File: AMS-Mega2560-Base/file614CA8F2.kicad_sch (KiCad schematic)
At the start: 22 parts, among them IC13 MAX764CPA+, IC14 LM2917N-8_NOPB, J23 Conn_01x02, J24 Conn_01x02, J31 Conn_01x02, K1 DIP05-1A72-12L, Q25 2N7000

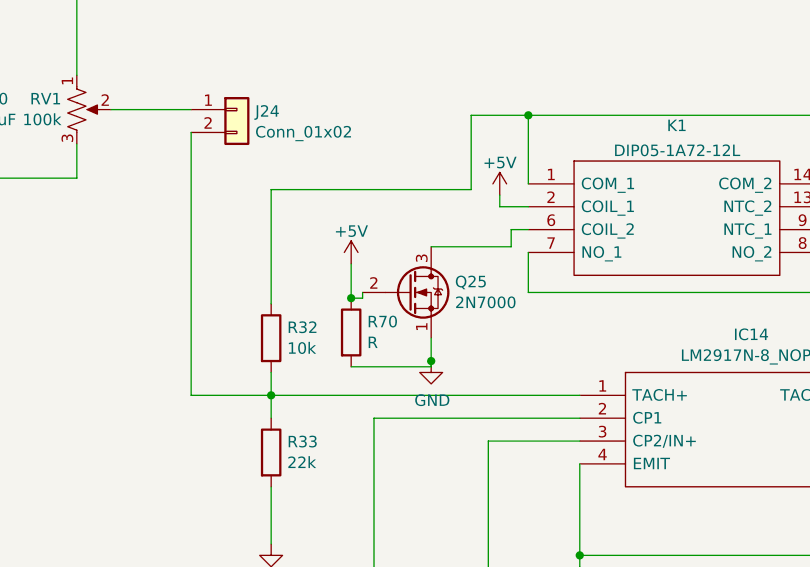
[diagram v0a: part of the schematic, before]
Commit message: applying some fixes for the RPM sensor and other parts of the schem
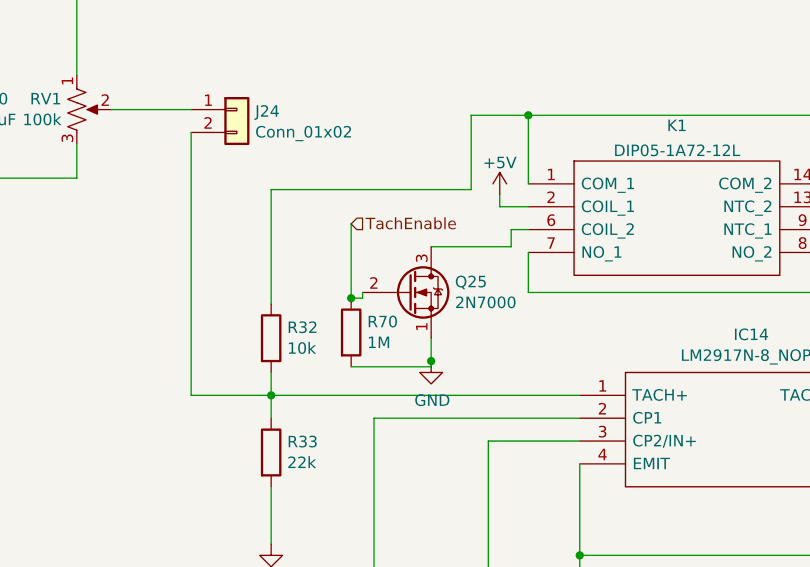
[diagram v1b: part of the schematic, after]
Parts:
- R70: value R -> 1M
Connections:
- net +5V: no longer Q25.2 (G), R70.1
- new net TachEnable: Q25.2 (G), R70.1
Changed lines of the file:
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@@
     (stroke (width 0) (type default) (color 0 0 0 0))
   )
-  (wire (pts (xy 161.29 79.375) (xy 161.29 83.185))
+  (wire (pts (xy 161.29 74.93) (xy 161.29 83.185))
     (stroke (width 0) (type default) (color 0 0 0 0))
   )
@@
   )
   (hierarchical_label "TachIn" (shape input) (at 219.075 78.105 0)
+    (effects (font (size 1.27 1.27)) (justify left))
+  )
+  (hierarchical_label "TachEnable" (shape input) (at 161.29 74.93 0)
     (effects (font (size 1.27 1.27)) (justify left))
   )
@@
       (effects (font (size 1.27 1.27)) (justify left))
     )
-    (property "Value" "R" (id 1) (at 163.068 88.138 0)
+    (property "Value" "1M" (id 1) (at 163.068 88.138 0)
       (effects (font (size 1.27 1.27)) (justify left))
     )
@@
     (pin "9")
   )
-  (symbol (lib_id "power:+5V") (at 161.29 79.375 0) (unit 1)
-    (in_bom yes) (on_board yes) (fields_autoplaced)
-    (property "Reference" "#PWR038" (id 0) (at 161.29 83.185 0)
-      (effects (font (size 1.27 1.27)) hide)
-    )
-    (property "Value" "+5V" (id 1) (at 161.29 75.7705 0))
-    (property "Footprint" "" (id 2) (at 161.29 79.375 0)
-      (effects (font (size 1.27 1.27)) hide)
-    )
-    (property "Datasheet" "" (id 3) (at 161.29 79.375 0)
-      (effects (font (size 1.27 1.27)) hide)
-    )
-    (pin "1")
-  )
 )

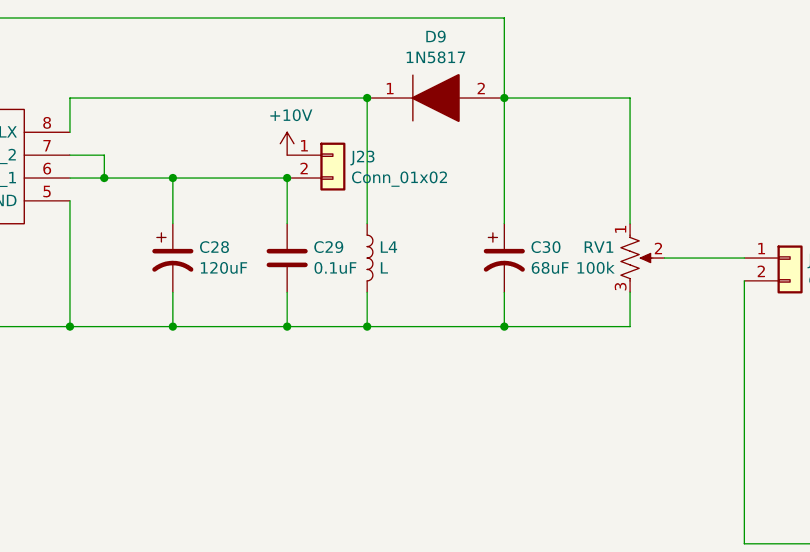
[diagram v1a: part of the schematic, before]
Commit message: updating some values and footprints. needs to have the routing tweaked
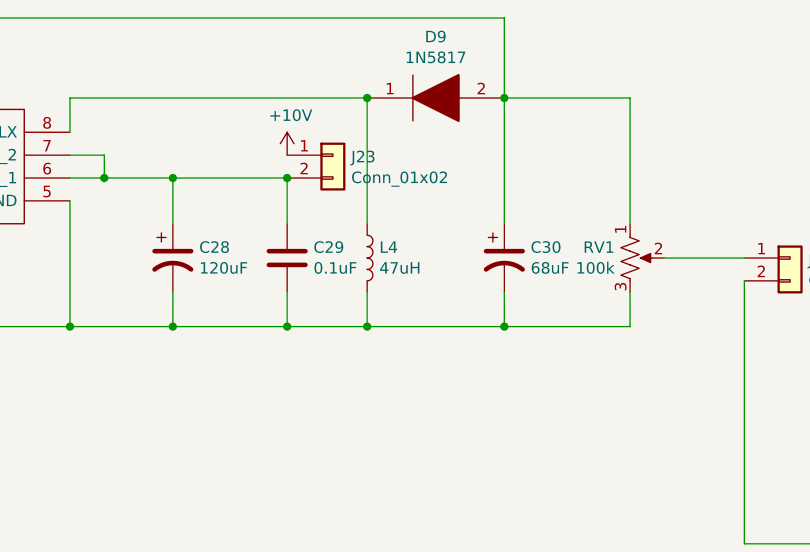
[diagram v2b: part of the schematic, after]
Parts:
- C28, C30: footprint Capacitor_THT:CP_Radial_D10.0mm_P5.00mm -> Capacitor_THT:CP_Radial_D8.0mm_P5.00mm
- C32: footprint Capacitor_THT:CP_Radial_D7.5mm_P2.50mm -> Capacitor_THT:C_Radial_D4.0mm_H5.0mm_P1.50mm
- L4: value L -> 47uH
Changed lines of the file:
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@@
       (effects (font (size 1.27 1.27)) (justify left))
     )
-    (property "Footprint" "Capacitor_THT:CP_Radial_D10.0mm_P5.00mm" (id 2) (at 116.84 62.23 0)
+    (property "Footprint" "Capacitor_THT:CP_Radial_D8.0mm_P5.00mm" (id 2) (at 116.84 62.23 0)
       (effects (font (size 1.27 1.27)) hide)
     )
@@
       (effects (font (size 1.27 1.27)) (justify left))
     )
-    (property "Footprint" "Capacitor_THT:CP_Radial_D10.0mm_P5.00mm" (id 2) (at 80.01 62.23 0)
+    (property "Footprint" "Capacitor_THT:CP_Radial_D8.0mm_P5.00mm" (id 2) (at 80.01 62.23 0)
       (effects (font (size 1.27 1.27)) hide)
     )
@@
       (effects (font (size 1.27 1.27)) (justify left))
     )
-    (property "Value" "L" (id 1) (at 102.9462 63.373 0)
+    (property "Value" "47uH" (id 1) (at 102.9462 63.373 0)
       (effects (font (size 1.27 1.27)) (justify left))
     )
@@
       (effects (font (size 1.27 1.27)) (justify left))
     )
-    (property "Footprint" "Capacitor_THT:CP_Radial_D7.5mm_P2.50mm" (id 2) (at 166.37 125.73 0)
-      (effects (font (size 1.27 1.27)) hide)
-    )
+    (property "Footprint" "Capacitor_THT:C_Radial_D4.0mm_H5.0mm_P1.50mm" (id 2) (at 166.37 125.73 0)
+      (effects (font (size 1.27 1.27)) hide)
+    )
